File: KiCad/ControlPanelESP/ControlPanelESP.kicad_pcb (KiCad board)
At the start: 4 copper layers, 116.4 x 29 mm, 39 parts, among them J1 Conn_01x02_Male, J2 Conn_01x06_Male, J4 Conn_01x03_Male, J5 Conn_01x02_Male, J7 Conn_01x02_Male, K1 DIPxx-1Axx-11x, Q1 Q_NPN_BEC, Q2 Q_NPN_BEC, Q3 Q_NMOS_GSD, Q4 Q_NMOS_GSD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

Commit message: second version
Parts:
- added C8: C_Polarized, Capacitor_THT:CP_Radial_D5.0mm_P2.00mm, F.Cu at (51.7, 80.8)
- added C9: C_Polarized, Capacitor_THT:CP_Radial_D5.0mm_P2.00mm, F.Cu at (51.7, 88.4)
- moved D1 33.6 mm to (68.1, 100.7)
- moved C1 11.0 mm to (40.5, 81.0), turned to -90 degrees
- moved R3 11.0 mm to (48.8, 90.8)
- moved C2 9.12 mm to (47.1, 88.4), turned to 180 degrees
- moved U1 2.09 mm to (45.1, 83.2), turned to -90 degrees
- moved H4 1.42 mm to (52.5, 92.7)
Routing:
- net +3V3: track 50.0 -> 75.4 mm, vias 2 -> 3
- net Net-(D1-Pad2): track 2.43 -> 25.7 mm, vias 0 -> 2
- net 5V: track 141.7 -> 159.5 mm
- net Net-(R7-Pad2): track 14.6 -> 7.45 mm, vias 2 -> 1
- net EN: track 59.9 -> 58.9 mm
- net LED: track 81.0 -> 80.2 mm
- net Net-(J5-Pad2): track 17.4 -> 16.6 mm
- net Net-(K1-Pad2): track 67.3 -> 66.7 mm
- net RTS: track 37.6 -> 37.0 mm
- net GND: track 37.2 -> 37.3 mm, vias 9 -> 11
- added copper zone on In2.Cu, net +3V3
- added copper zone on In1.Cu, net 5V
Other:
- board text added: "230V"
- board text added: "5V"
- board text added: "5V PWR IN"
- board text added: "BOOT"
- board text added: "DIM"
- board text added: "DTR"
- board text added: "FAN"
- board text added: "GND"
- board text added: "RST"
- board text added: "RTS"
- board text added: "RX"
- board text added: "TX"
- board text added: "|"

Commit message: V2.0 of PCB
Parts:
- removed D1: LED, LED_SMD:LED_0805_2012Metric_Pad1.15x1.40mm_HandSolder
- removed Q1, Q2: Q_NPN_BEC, Package_TO_SOT_SMD:SOT-23
- added H5: MountingHole_Pad, MountingHole:MountingHole_2.2mm_M2_DIN965_Pad, F.Cu at (77.3, 91.7)
- added IC1: MCP3221A6T-E_OT, Samacsys:SOT95P280X145-5N, F.Cu at (52.4, 83.8)
- added J3: Conn_01x04_Male, Connector_PinHeader_2.54mm:PinHeader_1x04_P2.54mm_Vertical, F.Cu at (45.7, 87.4)
- added J6: Conn_01x03_Male, Connector_PinHeader_2.54mm:PinHeader_1x03_P2.54mm_Vertical, F.Cu at (43.2, 83.8)
- added R12: 4k7, Resistor_SMD:R_0805_2012Metric_Pad1.20x1.40mm_HandSolder, F.Cu at (69.6, 100.6)
- added U4: LM4040DIM3X-4.1, Package_TO_SOT_SMD:SOT-23, F.Cu at (48.4, 90.5)
- J1, J5: footprint Connector_JST:JST_XH_B2B-XH-A_1x02_P2.50mm_Vertical -> Connector_PinHeader_2.54mm:PinHeader_1x02_P2.54mm_Vertical
- J2: value Conn_01x06_Male -> Conn_01x04_Male; footprint Connector_JST:JST_XH_B6B-XH-A_1x06_P2.50mm_Vertical -> Connector_PinHeader_2.54mm:PinHeader_1x04_P2.54mm_Vertical
- J4: value Conn_01x03_Male -> Conn_01x02_Male; footprint Connector_JST:JST_XH_B3B-XH-A_1x03_P2.50mm_Vertical -> Connector_PinHeader_2.54mm:PinHeader_1x02_P2.54mm_Vertical
- J7: value Conn_01x02_Male -> 2086-3122; footprint Connector_JST:JST_XH_B2B-XH-A_1x02_P2.50mm_Vertical -> Lichtwecker:2086-3122
- R2: value 10k -> 1k
- R3: value 1k -> 4k7
- R6: value 4k7 -> 5.1k
- moved C1 81.0 mm to (121.5, 82.9), turned to 90 degrees
- moved U1 73.5 mm to (118.4, 88.3), turned to 180 degrees
- moved C8 72.9 mm to (124.5, 84.5), turned to 0 degrees
- moved J2 68.4 mm to (43.2, 80.3), turned to 90 degrees
- moved C2 66.0 mm to (112.6, 80.8), turned to 90 degrees
- moved C9 64.9 mm to (116.3, 81.8), turned to 0 degrees
- moved R1 64.0 mm to (62.2, 99.3), turned to 180 degrees
- moved R2 61.8 mm to (52.1, 89.7), turned to 180 degrees
- moved R11 51.9 mm to (129.8, 88.4), turned to 90 degrees
- moved Q5 49.2 mm to (126.7, 89.0), turned to 180 degrees
- moved R6 41.9 mm to (39.6, 80.8), turned to -90 degrees
- moved H1 36.4 mm to (112.5, 104.9)
- moved C4 33.7 mm to (111.5, 85.9), turned to 90 degrees
- moved R4 32.0 mm to (111.5, 89.9)
- moved C3 23.9 mm to (109.5, 83.8), turned to 90 degrees
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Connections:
- H1 pad 1: GND -> unconnected-(H1-Pad1)
- H2 pad 1: GND -> unconnected-(H2-Pad1)
- H3 pad 1: GND -> unconnected-(H3-Pad1)
- H4 pad 1: GND -> unconnected-(H4-Pad1)
- J7 pad 1: Net-(J7-Pad1) -> /230V
- J7 pad 2: Net-(J7-Pad2) -> /230V1
- K1 pad 1: Net-(J7-Pad1) -> /230V1
- K1 pad 7: Net-(J7-Pad2) -> /230V
- R1 pad 1: DTR -> +3V3
- R1 pad 2: Net-(Q1-Pad1) -> IO0
- R2 pad 1: Net-(Q2-Pad1) -> 5V
- R2 pad 2: RTS -> Net-(IC1-Pad1)
- R3 pad 2: Net-(D1-Pad2) -> SDA
- R6 pad 2: DS18B20 -> TEMPSENSOR
- U2 pad 13: DS18B20 -> unconnected-(U2-Pad13)
- U2 pad 33: unconnected-(U2-Pad33) -> SDA
- U2 pad 36: unconnected-(U2-Pad36) -> SCL
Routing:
- net 5V: track 159.5 -> 53.3 mm, vias 4 -> 3
- net Relay: track 24.0 -> 80.2 mm, vias 0 -> 3
- net Net-(K1-Pad2): track 66.7 -> 10.6 mm, vias 2 -> 0
- net DTR: track 42.0 -> 0.00 mm, vias 3 -> 0
- net +3V3: track 75.4 -> 37.5 mm, vias 3 -> 15
- net RTS: track 37.0 -> 0.00 mm, vias 3 -> 0
- net Net-(Q2-Pad1): track 34.5 -> 0.00 mm, vias 2 -> 0
- net Net-(Q1-Pad1): track 33.9 -> 0.00 mm, vias 2 -> 0
- net TX_ESP32: track 61.2 -> 27.7 mm, vias 1 -> 2
- net GND: track 37.3 -> 4.61 mm, vias 11 -> 14
- net RX_ESP32: track 59.8 -> 29.0 mm, vias 1 -> 2
- net SCL: track 0.00 -> 29.5 mm, vias 0 -> 2
- net DS18B20: track 26.4 -> 0.00 mm, vias 2 -> 0
- net Net-(D1-Pad2): track 25.7 -> 0.00 mm, vias 2 -> 0
- net SDA: track 0.00 -> 22.7 mm, vias 0 -> 2
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- added copper zone on F.Cu, net +3V3
- added copper zone on In1.Cu, net +3V3
- added copper zone on B.Cu, net 5V
- added copper zone on F.Cu, net 5V
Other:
- board text removed: "230V"
- board text removed: "5V"
- board text removed: "5V PWR IN"
- board text removed: "DIM"
- board text removed: "DTR"
- board text removed: "FAN"
- board text removed: "GND"
- board text removed: "RTS"
- board text removed: "RX"
- board text removed: "TX"
- board text removed: "|"

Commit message: finalized PCB
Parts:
- moved R12 1.40 mm to (71.0, 100.6)
- moved R4 0.85 mm to (111.9, 89.2), turned to 180 degrees
- moved R7 0.25 mm to (116.3, 92.7)
- moved R3 0.13 mm to (67.2, 100.6)
- moved H5 0.13 mm to (77.5, 91.7)
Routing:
- net Relay: track 80.2 -> 86.6 mm
- net BUTTON: track 36.9 -> 39.9 mm
- net +3V3: track 37.5 -> 35.4 mm
- net GND: vias 14 -> 19

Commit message: finalized PCB again
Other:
- board text added: "230V"
- board text added: "5V PWR"
- board text added: "BUTTON"
- board text added: "DIM"
- board text added: "FAN"
- board text added: "PROG"
- board text added: "RGB"
- board text added: "TS"
- board text added: "VinFar ESP32-Lichtwecker V2.0"
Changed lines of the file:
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@@
     (property "Sheetname" "")
     (attr smd)
-    (fp_text reference "IC1" (at 0 0) (layer "F.SilkS")
-      (effects (font (size 1.27 1.27) (thickness 0.254)))
+    (fp_text reference "IC1" (at 1.6764 -2.54 270) (layer "F.SilkS")
+      (effects (font (size 1 1) (thickness 0.15)))
     )
     (fp_text value "MCP3221A6T-E_OT" (at 0 0) (layer "F.SilkS") hide
@@
       (effects (font (size 1.27 1.27) (thickness 0.254)))
     )
-    (fp_line (start -0.3 -1.475) (end 0.3 -1.475) (layer "F.SilkS") (width 0.2))
     (fp_line (start -0.3 1.475) (end -0.3 -1.475) (layer "F.SilkS") (width 0.2))
     (fp_line (start 0.3 -1.475) (end 0.3 1.475) (layer "F.SilkS") (width 0.2))
+    (fp_line (start -1.85 -1.5) (end -0.65 -1.5) (layer "F.SilkS") (width 0.2))
+    (fp_line (start -0.3 -1.475) (end 0.3 -1.475) (layer "F.SilkS") (width 0.2))
     (fp_line (start 0.3 1.475) (end -0.3 1.475) (layer "F.SilkS") (width 0.2))
-    (fp_line (start -1.85 -1.5) (end -0.65 -1.5) (layer "F.SilkS") (width 0.2))
+    (fp_line (start -2.1 -1.8) (end 2.1 -1.8) (layer "F.CrtYd") (width 0.05))
     (fp_line (start 2.1 -1.8) (end 2.1 1.8) (layer "F.CrtYd") (width 0.05))
+    (fp_line (start 2.1 1.8) (end -2.1 1.8) (layer "F.CrtYd") (width 0.05))
     (fp_line (start -2.1 1.8) (end -2.1 -1.8) (layer "F.CrtYd") (width 0.05))
-    (fp_line (start -2.1 -1.8) (end 2.1 -1.8) (layer "F.CrtYd") (width 0.05))
-    (fp_line (start 2.1 1.8) (end -2.1 1.8) (layer "F.CrtYd") (width 0.05))
     (fp_line (start -0.812 1.475) (end -0.812 -1.475) (layer "F.Fab") (width 0.1))
-    (fp_line (start -0.812 -0.525) (end 0.138 -1.475) (layer "F.Fab") (width 0.1))
+    (fp_line (start 0.812 1.475) (end -0.812 1.475) (layer "F.Fab") (width 0.1))
     (fp_line (start -0.812 -1.475) (end 0.812 -1.475) (layer "F.Fab") (width 0.1))
     (fp_line (start 0.812 -1.475) (end 0.812 1.475) (layer "F.Fab") (width 0.1))
-    (fp_line (start 0.812 1.475) (end -0.812 1.475) (layer "F.Fab") (width 0.1))
-    (pad "1" smd rect locked (at -1.25 -0.95 90) (size 0.6 1.2) (layers "F.Cu" "F.Paste" "F.Mask")
+    (fp_line (start -0.812 -0.525) (end 0.138 -1.475) (layer "F.Fab") (width 0.1))
+    (pad "1" smd rect (at -1.25 -0.95 90) (size 0.6 1.2) (layers "F.Cu" "F.Paste" "F.Mask")
       (net 33 "Net-(IC1-Pad1)") (pinfunction "VDD") (pintype "passive"))
-    (pad "2" smd rect locked (at -1.25 0 90) (size 0.6 1.2) (layers "F.Cu" "F.Paste" "F.Mask")
+    (pad "2" smd rect (at -1.25 0 90) (size 0.6 1.2) (layers "F.Cu" "F.Paste" "F.Mask")
       (net 2 "GND") (pinfunction "VSS") (pintype "passive"))
-    (pad "3" smd rect locked (at -1.25 0.95 90) (size 0.6 1.2) (layers "F.Cu" "F.Paste" "F.Mask")
+    (pad "3" smd rect (at -1.25 0.95 90) (size 0.6 1.2) (layers "F.Cu" "F.Paste" "F.Mask")
       (net 34 "TEMPSENSOR") (pinfunction "AIN") (pintype "passive"))
-    (pad "4" smd rect locked (at 1.25 0.95 90) (size 0.6 1.2) (layers "F.Cu" "F.Paste" "F.Mask")
+    (pad "4" smd rect (at 1.25 0.95 90) (size 0.6 1.2) (layers "F.Cu" "F.Paste" "F.Mask")
       (net 36 "SDA") (pinfunction "SDA") (pintype "passive"))
-    (pad "5" smd rect locked (at 1.25 -0.95 90) (size 0.6 1.2) (layers "F.Cu" "F.Paste" "F.Mask")
+    (pad "5" smd rect (at 1.25 -0.95 90) (size 0.6 1.2) (layers "F.Cu" "F.Paste" "F.Mask")
       (net 37 "SCL") (pinfunction "SCL") (pintype "passive"))
     (model "C:\\Users\\Vincent\\Documents\\GitHub\\MyKiCadLibrary\\SamacSys_Parts.3dshapes\\MCP3221A6T-E_OT.stp"
@@
     (property "Sheetname" "")
     (attr through_hole)
-    (fp_text reference "J1" (at 0.6858 -2.154 180) (layer "F.SilkS")
+    (fp_text reference "J1" (at 0.8128 -2.916 180) (layer "F.SilkS")
       (effects (font (size 1 1) (thickness 0.15)))
     )
@@
     (property "Sheetname" "")
     (attr smd)
-    (fp_text reference "U2" (at 10.176 -9.645 90) (layer "F.SilkS")
+    (fp_text reference "U2" (at 5.604 -10.407 90) (layer "F.SilkS")
       (effects (font (size 0.75 0.75) (thickness 0.1)))
     )
@@
     (property "Sheetname" "")
     (attr through_hole)
-    (fp_text reference "J5" (at 2.159 1.905 180) (layer "F.SilkS")
+    (fp_text reference "J5" (at 0 5.334 180) (layer "F.SilkS")
       (effects (font (size 1 1) (thickness 0.15)))
     )
@@
     (property "Sheetname" "")
     (attr smd)
-    (fp_text reference "U4" (at 2.1844 0.8636) (layer "F.SilkS")
+    (fp_text reference "U4" (at 2.1844 0.9906) (layer "F.SilkS")
       (effects (font (size 1 1) (thickness 0.15)))
     )
@@
     (property "Sheetname" "")
     (attr through_hole)
-    (fp_text reference "K1" (at 13.8568 0.3172 180) (layer "F.SilkS")
+    (fp_text reference "K1" (at 13.425 1.892 270) (layer "F.SilkS")
       (effects (font (size 1 1) (thickness 0.15)))
     )
@@
     (property "Sheetname" "")
     (attr through_hole)
-    (fp_text reference "J4" (at 2.1844 2.6974 180) (layer "F.SilkS")
+    (fp_text reference "J4" (at 0 -2.667 180) (layer "F.SilkS")
       (effects (font (size 1 1) (thickness 0.15)))
     )
@@
     )
   )
+  (gr_line (start 119.38 99.822) (end 121.92 99.822) (layer "F.SilkS") (width 0.3))
+  (gr_line (start 113.665 99.822) (end 116.205 99.822) (layer "F.SilkS") (width 0.3))
   (gr_arc (start 80.01 92.558567) (mid 79.526433 93.726) (end 78.359 94.209567) (layer "Edge.Cuts") (width 0.1))
   (gr_arc (start 152.237244 78.877571) (mid 153.176381 79.586844) (end 152.92392 80.736326) (layer "Edge.Cuts") (width 0.05))
@@
   (gr_line (start 80.899 85.725) (end 108.585 85.725) (layer "Edge.Cuts") (width 0.1))
   (gr_arc (start 111.163599 107.744055) (mid 110.382366 107.68375) (end 109.982 107.010201) (layer "Edge.Cuts") (width 0.05))
+  (gr_text "VinFar ESP32-Lichtwecker V2.0" (at 95.885 84.328) (layer "B.SilkS")
+    (effects (font (size 1.5 1.5) (thickness 0.225)) (justify mirror))
+  )
+  (gr_text "BUTTON" (at 45.72 82.042) (layer "F.SilkS")
+    (effects (font (size 0.6 0.6) (thickness 0.09)))
+  )
+  (gr_text "PROG" (at 52.959 80.391 90) (layer "F.SilkS")
+    (effects (font (size 0.75 0.75) (thickness 0.1)))
+  )
   (gr_text "BOOT" (at 96.841803 82.620621 90) (layer "F.SilkS")
     (effects (font (size 0.75 0.75) (thickness 0.1)))
   )
+  (gr_text "FAN" (at 120.523 103.886) (layer "F.SilkS")
+    (effects (font (size 1 1) (thickness 0.15)))
+  )
+  (gr_text "230V" (at 142.113 89.027 90) (layer "F.SilkS")
+    (effects (font (size 1 1) (thickness 0.15)))
+  )
+  (gr_text "DIM" (at 115.824 103.886) (layer "F.SilkS")
+    (effects (font (size 1 1) (thickness 0.15)))
+  )
+  (gr_text "5V PWR	" (at 128.778 80.264 90) (layer "F.SilkS")
+    (effects (font (size 0.5 0.5) (thickness 0.075)))
+  )
   (gr_text "RST" (at 107.442 82.55 90) (layer "F.SilkS")
     (effects (font (size 0.75 0.75) (thickness 0.1)))
   )
+  (gr_text "RGB" (at 48.387 85.598) (layer "F.SilkS")
+    (effects (font (size 0.75 0.75) (thickness 0.1)))
+  )
+  (gr_text "TS" (at 50.8 85.598) (layer "F.SilkS")
+    (effects (font (size 0.75 0.75) (thickness 0.1)))
+  )

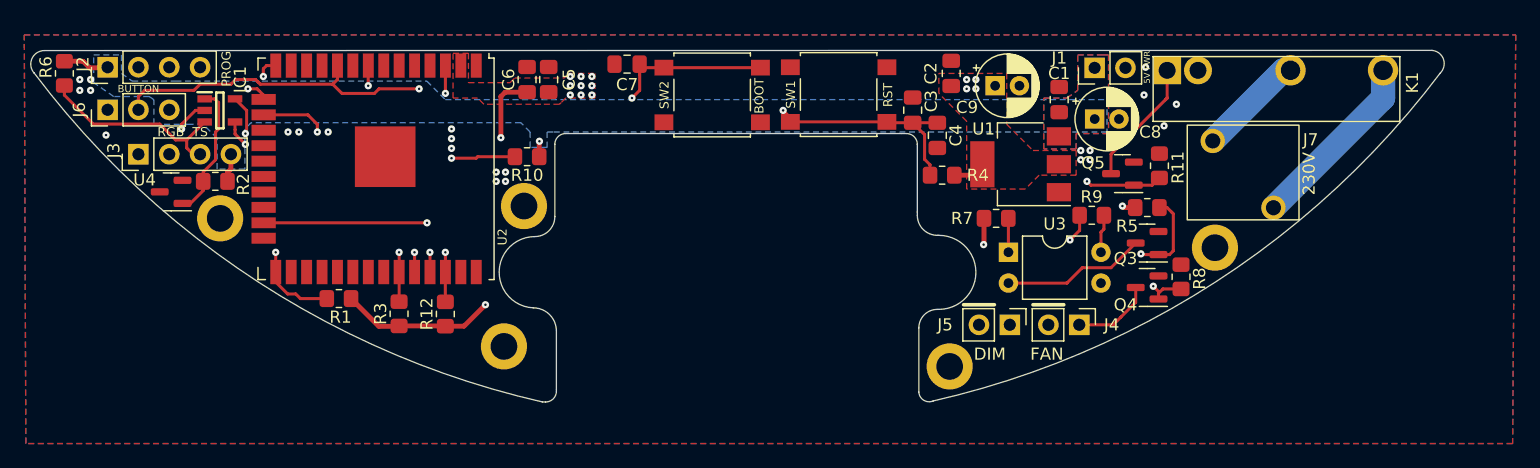
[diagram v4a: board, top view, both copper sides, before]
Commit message: add: OLED Display Connector, some markers
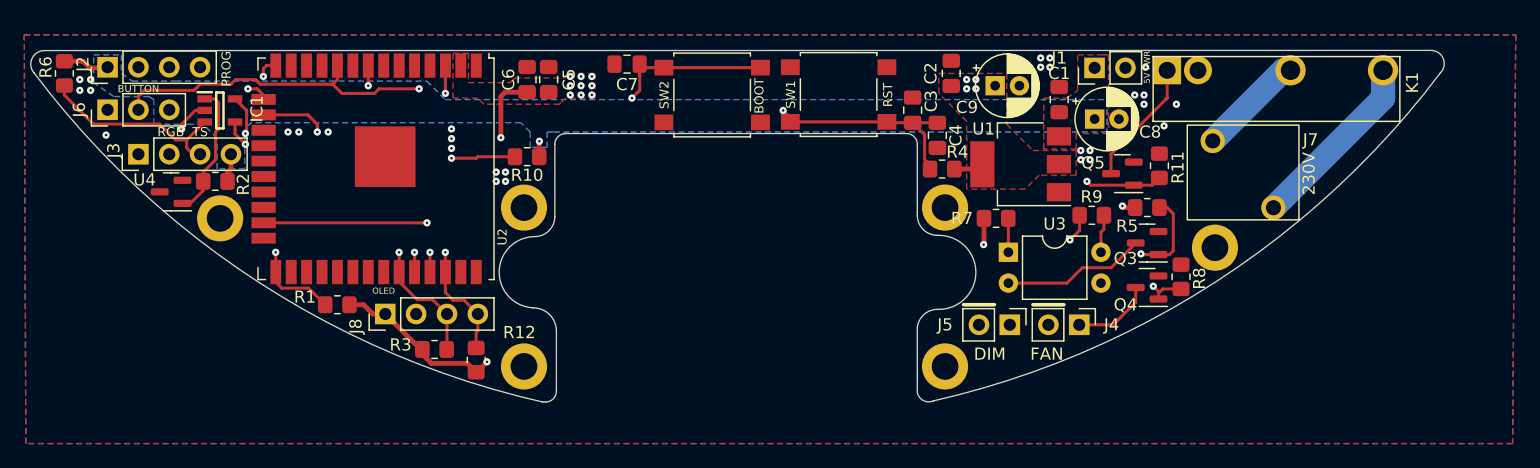
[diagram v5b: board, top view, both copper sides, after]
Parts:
- added H6: MountingHole_Pad, MountingHole:MountingHole_2.2mm_M2_DIN965_Pad, F.Cu at (112.1, 91.8)
- added J8: Conn_01x04_Male, Connector_PinHeader_2.54mm:PinHeader_1x04_P2.54mm_Vertical, F.Cu at (66.0, 100.6)
- moved R12 4.57 mm to (73.5, 104.4)
- moved R3 4.14 mm to (70.1, 103.5), turned to 0 degrees
- moved H2 2.33 mm to (77.5, 104.9)
- moved R1 0.52 mm to (62.1, 99.8)
- moved R4 0.51 mm to (111.9, 88.6)
- moved H1 0.38 mm to (112.1, 104.9)
- moved H5 0.13 mm to (77.5, 91.8)
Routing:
- net SDA: track 22.5 -> 28.9 mm
- net +3V3: track 35.4 -> 41.8 mm
- net SCL: track 29.1 -> 34.6 mm
- net IO0: track 58.1 -> 59.0 mm
- net EN: track 48.6 -> 48.1 mm
- net GND: vias 19 -> 25
- added copper zone on In2.Cu, net 5V
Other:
- outline, holes or cut-outs redrawn
- board text added: "OLED"

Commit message: ch: MCP1541 as voltage reference for ADC
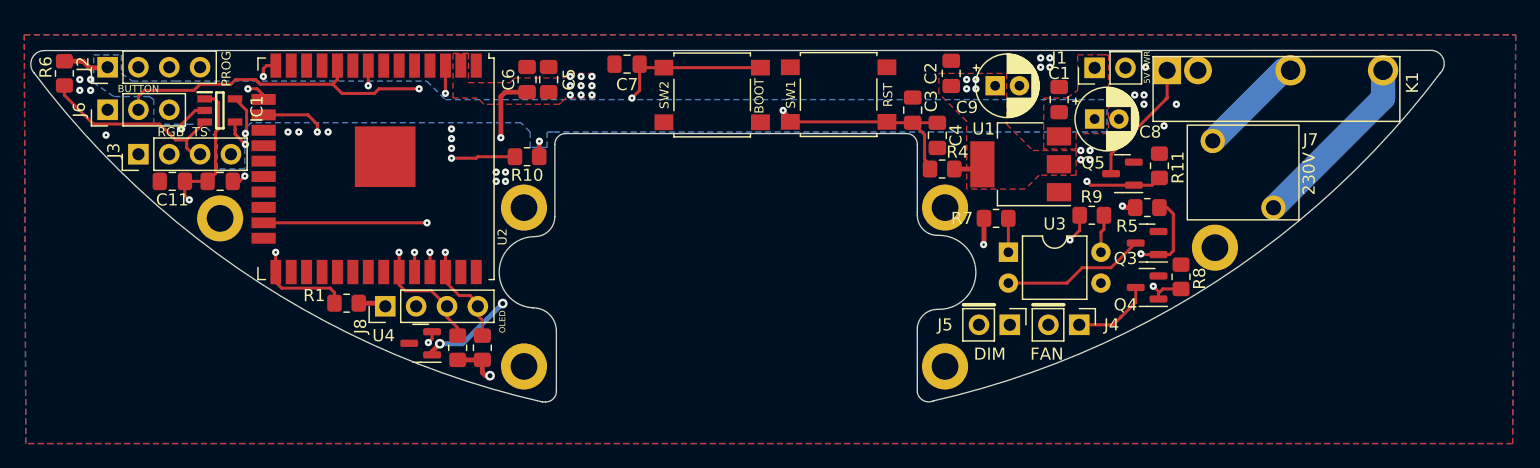
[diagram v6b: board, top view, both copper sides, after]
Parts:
- removed R2: 1k, Resistor_SMD:R_0805_2012Metric_Pad1.20x1.40mm_HandSolder
- added C10: 10u, Capacitor_SMD:C_0805_2012Metric_Pad1.18x1.45mm_HandSolder, F.Cu at (52.5, 89.7)
- added C11: 100n, Capacitor_SMD:C_0805_2012Metric_Pad1.18x1.45mm_HandSolder, F.Cu at (48.5, 89.7)
- U4: value LM4040DIM3X-4.1 -> MCP1541-TT
- moved U4 24.0 mm to (69.0, 103.0)
- moved R3 1.91 mm to (72.0, 103.4), turned to 90 degrees
- moved R12 1.14 mm to (74.0, 103.4)
- moved R1 0.77 mm to (62.9, 99.7)
- moved J8 0.64 mm to (66.0, 99.9)
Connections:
- U4 pad 1: Net-(IC1-Pad1) -> 5V
- U4 pad 2: GND -> Net-(IC1-Pad1)
- U4 pad 3: (no net) -> GND
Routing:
- net Net-(IC1-Pad1): track 11.2 -> 38.2 mm, vias 0 -> 2
- net 5V: track 53.3 -> 75.7 mm, vias 3 -> 5
- net +3V3: track 41.8 -> 46.7 mm
- net IO0: track 59.0 -> 60.2 mm
- net GND: track 4.61 -> 5.78 mm, vias 25 -> 26
- net SCL: track 34.6 -> 33.6 mm
